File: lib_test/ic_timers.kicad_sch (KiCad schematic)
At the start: 1 part, among them X12001 16MHz

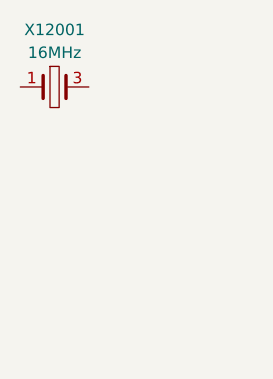
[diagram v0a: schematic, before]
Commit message: add NE555
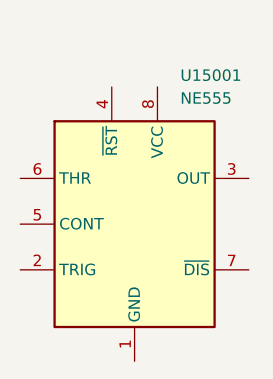
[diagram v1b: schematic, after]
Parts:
- removed X12001: 16MHz, lily_footprints:crystal_3225, symbol lily_symbols:crystal_16MHz_20ppm_8pF_3225
- added U15001: NE555, lily_footprints:soic8, symbol lily_symbols:ic_timer_NE555_soic8
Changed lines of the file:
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@@
 	)
 	(symbol
-		(lib_id "lily_symbols:crystal_16MHz_20ppm_8pF_3225")
-		(at 25.4 25.4 0)
+		(lib_id "lily_symbols:ic_timer_NE555_soic8")
+		(at 25.4 35.56 0)
 		(unit 1)
 		(exclude_from_sim no)
@@
 		(on_board yes)
 		(dnp no)
-		(property "Reference" "X12001"
-			(at 29.21 19.05 0)
+		(property "Reference" "U15001"
+			(at 43.18 24.13 0)
 			(effects
 				(font
 					(size 1.27 1.27)
 				)
+				(justify left)
 			)
 		)
-		(property "Value" "16MHz"
-			(at 29.21 21.59 0)
+		(property "Value" "NE555"
+			(at 43.18 26.67 0)
 			(effects
 				(font
 					(size 1.27 1.27)
 				)
+				(justify left)
 			)
 		)
-		(property "Footprint" "lily_footprints:crystal_3225"
-			(at 29.21 35.56 0)
+		(property "Footprint" "lily_footprints:soic8"
+			(at 38.1 73.66 0)
 			(effects
 				(font
@@
 		)
 		(property "Datasheet" ""
-			(at 20.32 17.78 0)
+			(at 25.4 35.56 0)
 			(effects
 				(font
@@
 		)
 		(property "Description" ""
-			(at 25.4 25.4 0)
+			(at 25.4 35.56 0)
 			(effects
 				(font
@@
 		)
 		(property "Revision" "1"
-			(at 29.21 30.48 0)
+			(at 38.1 68.58 0)
 			(effects
 				(font
@@
 		)
 		(property "Status" "Active"
-			(at 29.21 33.02 0)
+			(at 38.1 71.12 0)
 			(effects
 				(font
@@
 			)
 		)
-		(property "Manufacturer" "NDK"
-			(at 29.21 38.1 0)
+		(property "Manufacturer" "IDCHIP"
+			(at 38.1 76.2 0)
 			(effects
 				(font
@@
 			)
 		)
-		(property "Manufacturer_ID" "NX3225GA-16MHZ-STD-CRG-2"
-			(at 29.21 40.64 0)
+		(property "Manufacturer_ID" "NE555"
+			(at 38.1 78.74 0)
 			(effects
 				(font
@@
 			)
 		)
-		(property "Lily_ID" "1917-10002"
-			(at 28.575 43.18 0)
+		(property "Lily_ID" "1914-10012"
+			(at 38.1 81.28 0)
 			(effects
 				(font
@@
 			)
 		)
-		(property "JLCPCB_ID" "C156247"
-			(at 29.21 45.72 0)
+		(property "JLCPCB_ID" "C5125085"
+			(at 38.1 83.82 0)
 			(effects
 				(font
@@
 		)
 		(property "JLCPCB_STATUS" "Extended"
-			(at 29.21 48.26 0)
+			(at 38.1 86.36 0)
 			(effects
 				(font
@@
 			)
 		)
+		(pin "6"
+		)
+		(pin "5"
+		)
+		(pin "7"
+		)
 		(pin "2"
 		)
 		(pin "1"
 		)
+		(pin "3"
+		)
 		(pin "4"
 		)
-		(pin "3"
+		(pin "8"
 		)
 		(instances
 			(project "kicad_lib_test"
-				(path "/032b8f2d-5c08-4381-9e3a-c197ca84e3c5/a36be8d0-bc3d-4973-a559-35501cde04f1"
-					(reference "X12001")
+				(path "/032b8f2d-5c08-4381-9e3a-c197ca84e3c5/a89ded65-6ba0-47b6-baaa-9b3f23dcb92f"
+					(reference "U15001")
 					(unit 1)
 				)
